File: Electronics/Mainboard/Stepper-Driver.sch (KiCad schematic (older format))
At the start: 1 part

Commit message: Reference schematic
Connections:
- net GND: now reaches A1.1 (GND)
- net GND: now also A1.7 (GND)
- net VDD: now reaches A1.2 (VDD)
- net A+: now reaches A1.3 (1B)
- net A-: now reaches A1.4 (1A)
- net B+: now reaches A1.5 (2A)
- net B-: now reaches A1.6 (2B)
- net VMOT: now reaches A1.8 (VMOT)
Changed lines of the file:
@@
 $Descr A4 11693 8268
 encoding utf-8
-Sheet 8 11
+Sheet 3 11
 Title ""
 Date ""
@@
 AR Path="/5ED3A396" Ref="A?"  Part="1"
 AR Path="/5ED2FDF6/5ED3A396" Ref="A1"  Part="1"
-F 0 "A1" H 5850 4981 50  0000 C CNN
-F 1 "Pololu_Breakout_A4988" H 5850 4890 50  0000 C CNN
+F 0 "A1" H 6650 4900 50  0000 C CNN
+F 1 "Pololu_Breakout_A4988" H 6650 4800 50  0000 C CNN
 F 2 "Module:Pololu_Breakout-16_15.2x20.3mm" H 6075 3350 50  0001 L CNN
 F 3 "https://www.pololu.com/product/2980/pictures" H 5900 3800 50  0001 C CNN
@@
 	1    0    0    -1
 $EndComp
+Text HLabel 6450 4000 2    50   Output ~ 0
+A+
+Text HLabel 6450 4100 2    50   Output ~ 0
+A-
+Text HLabel 6450 4200 2    50   Output ~ 0
+B+
+Text HLabel 6450 4300 2    50   Output ~ 0
+B-
+Wire Wire Line
+	5800 4900 5800 5000
+Wire Wire Line
+	6000 4900 6000 5000
+Wire Wire Line
+	6000 5000 5800 5000
+Wire Wire Line
+	5800 5000 5700 5000
+Connection ~ 5800 5000
+Text HLabel 5700 5000 0    50   BiDi ~ 0
+GND
+Text HLabel 5800 3300 1    50   Input ~ 0
+VDD
+Text HLabel 6000 3300 1    50   Input ~ 0
+VMOT
+Wire Wire Line
+	6000 3300 6000 3400
+Wire Wire Line
+	5800 3400 5800 3300
+Wire Wire Line
+	6450 4000 6300 4000
+Wire Wire Line
+	6450 4100 6300 4100
+Wire Wire Line
+	6450 4200 6300 4200
+Wire Wire Line
+	6450 4300 6300 4300
 $EndSCHEMATC

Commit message: Reference layout finished
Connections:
- net STEP: now reaches A1.15 (STEP)
- net DIR: now reaches A1.16 (DIR)
- net ~ENABLE: now reaches A1.9 (~ENABLE)
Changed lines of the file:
@@
 Wire Wire Line
 	6450 4300 6300 4300
+Wire Wire Line
+	5400 4000 5300 4000
+Wire Wire Line
+	5300 4100 5400 4100
+Wire Wire Line
+	5400 4200 5300 4200
+Text HLabel 5300 4000 0    50   Input ~ 0
+~ENABLE
+Text HLabel 5300 4100 0    50   Input ~ 0
+STEP
+Text HLabel 5300 4200 0    50   Input ~ 0
+DIR
 $EndSCHEMATC

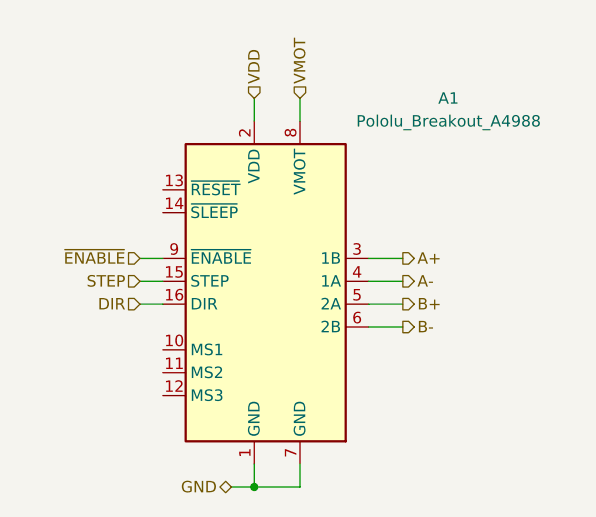
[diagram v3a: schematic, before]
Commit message: SPI Connections finished
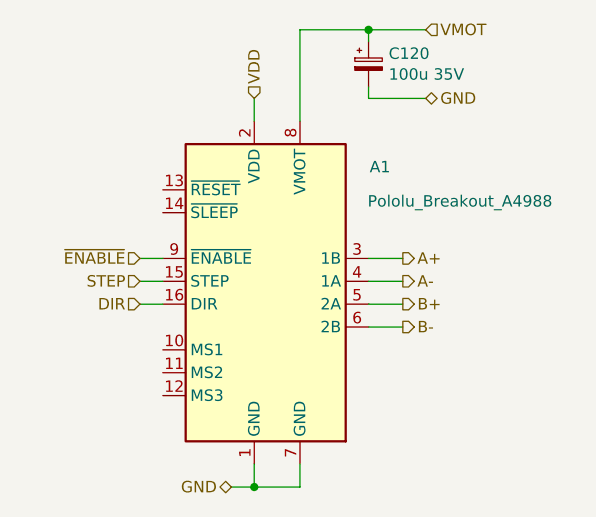
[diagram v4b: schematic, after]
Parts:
- added C120: 100u 35V, Capacitor_THT:CP_Radial_D6.3mm_P2.50mm, symbol Device:CP_Small
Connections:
- net GND: now also C120.2
- net VMOT: now also C120.1
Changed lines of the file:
@@
 AR Path="/5ED3A396" Ref="A?"  Part="1"
 AR Path="/5ED2FDF6/5ED3A396" Ref="A1"  Part="1"
-F 0 "A1" H 6650 4900 50  0000 C CNN
-F 1 "Pololu_Breakout_A4988" H 6650 4800 50  0000 C CNN
+F 0 "A1" H 6350 4600 50  0000 C CNN
+F 1 "Pololu_Breakout_A4988" H 6700 4450 50  0000 C CNN
 F 2 "Module:Pololu_Breakout-16_15.2x20.3mm" H 6075 3350 50  0001 L CNN
 F 3 "https://www.pololu.com/product/2980/pictures" H 5900 3800 50  0001 C CNN
@@
 Text HLabel 5800 3300 1    50   Input ~ 0
 VDD
-Text HLabel 6000 3300 1    50   Input ~ 0
+Text HLabel 6550 3000 2    50   Input ~ 0
 VMOT
-Wire Wire Line
-	6000 3300 6000 3400
 Wire Wire Line
 	5800 3400 5800 3300
@@
 Text HLabel 5300 4200 0    50   Input ~ 0
 DIR
+$Comp
+L Device:CP_Small C120
+U 1 1 5EF310A6
+P 6300 3150
+F 0 "C120" H 6388 3196 50  0000 L CNN
+F 1 "100u 35V" H 6388 3105 50  0000 L CNN
+F 2 "Capacitor_THT:CP_Radial_D6.3mm_P2.50mm" H 6300 3150 50  0001 C CNN
+F 3 "~" H 6300 3150 50  0001 C CNN
+	1    6300 3150
+	1    0    0    -1
+$EndComp
+Wire Wire Line
+	6000 3000 6300 3000
+Wire Wire Line
+	6300 3000 6300 3050
+Wire Wire Line
+	6000 3000 6000 3400
+Wire Wire Line
+	6300 3000 6550 3000
+Connection ~ 6300 3000
+Wire Wire Line
+	6300 3250 6300 3300
+Wire Wire Line
+	6300 3300 6550 3300
+Text HLabel 6550 3300 2    50   BiDi ~ 0
+GND
 $EndSCHEMATC

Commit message: Added images
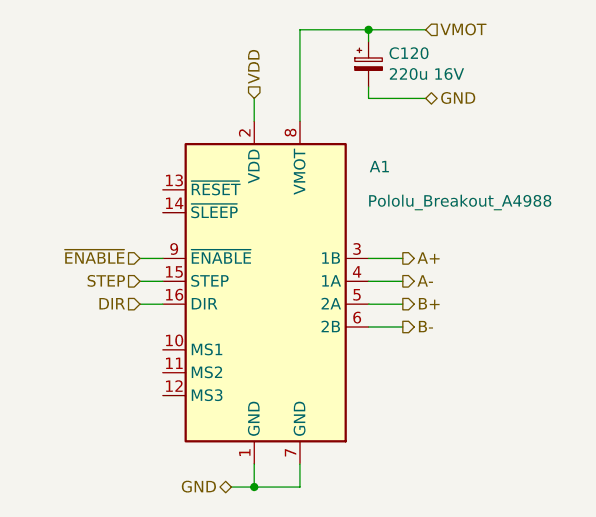
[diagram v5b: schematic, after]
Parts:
- C120: value 100u 35V -> 220u 16V; Reichelt (none) -> RAD FR 220/16
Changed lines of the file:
@@
 P 6300 3150
 F 0 "C120" H 6388 3196 50  0000 L CNN
-F 1 "100u 35V" H 6388 3105 50  0000 L CNN
+F 1 "220u 16V" H 6388 3105 50  0000 L CNN
 F 2 "Capacitor_THT:CP_Radial_D6.3mm_P2.50mm" H 6300 3150 50  0001 C CNN
 F 3 "~" H 6300 3150 50  0001 C CNN
+F 4 "RAD FR 220/16" H 6300 3150 50  0001 C CNN "Reichelt"
 	1    6300 3150
 	1    0    0    -1
